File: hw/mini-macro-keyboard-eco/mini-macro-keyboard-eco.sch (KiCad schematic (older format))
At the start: 39 parts, among them J0 USB, J1 DEBUG_SWD, SW0 BOOT, SW1 SW_Cherry_MX_1.00u_PCB, SW2 SW_Cherry_MX_1.00u_PCB, SW3 SW_Cherry_MX_1.00u_PCB, SW4 RESET, SW5 LAYOUT, SW6 BACKLIGHT, U1 USBLC6-2SC6, U2 XC6206P322MR, U3 STM32F070F6P6, Y1 16 MHz

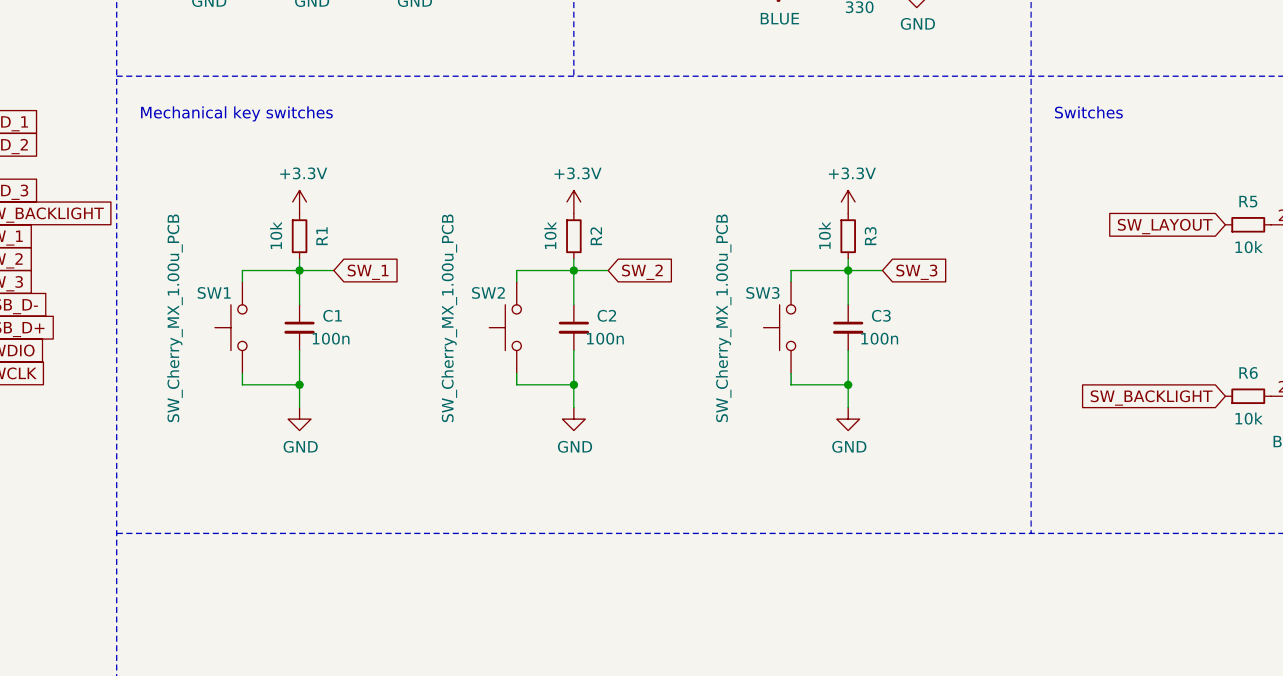
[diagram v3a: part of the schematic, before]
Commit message: fix(hw): remove debounce circuit from the mechanical switches
Signed-off-by: Ivan Kovalenko <s1ckretbox@gmail.com>
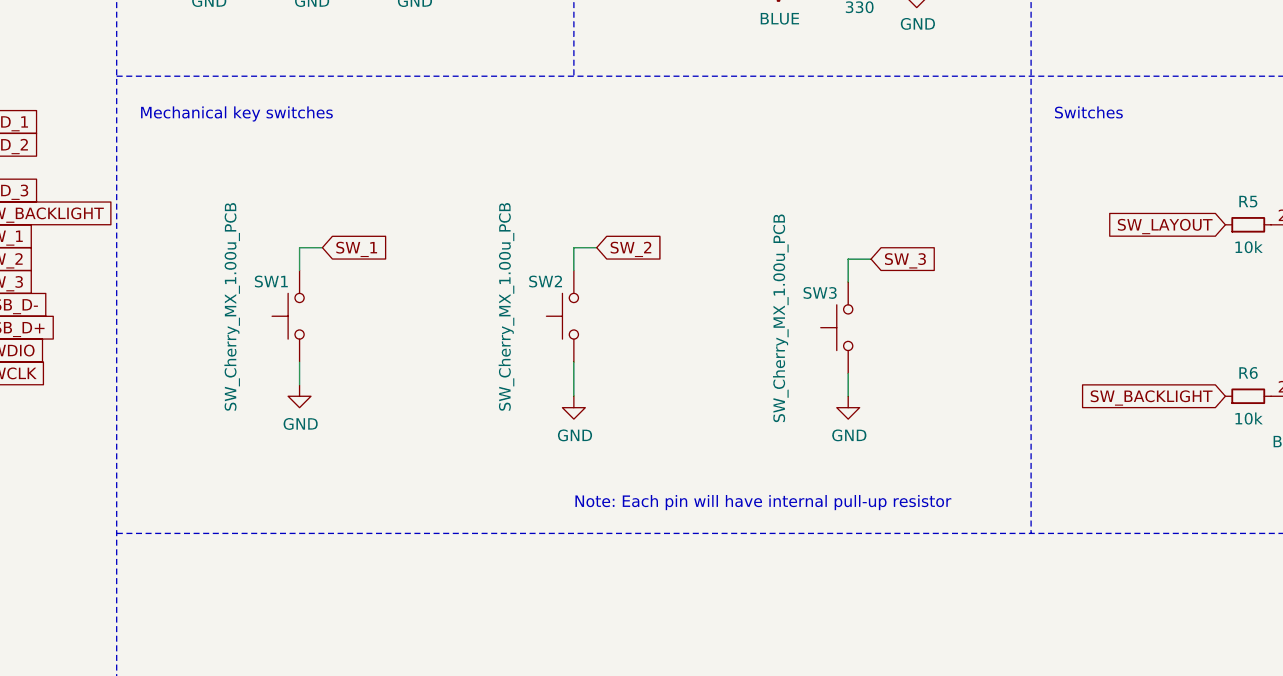
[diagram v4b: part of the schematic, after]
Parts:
- removed C1, C2, C3: 100n, Capacitor_SMD:C_0402_1005Metric, symbol mini-macro-keyboard-eco-rescue:C_Small-Device
- removed R1, R2, R3: 10k, Resistor_SMD:R_0402_1005Metric, symbol mini-macro-keyboard-eco-rescue:R_Small-Device
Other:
- note added: "Note: Each pin will have internal pull-up resistor"
- moved on the sheet: SW1, SW2, SW3
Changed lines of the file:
@@
 Wire Notes Line
 	5000 500  5000 7800
-Text GLabel 5950 2850 2    50   Input ~ 0
+Text GLabel 5900 2750 2    50   Input ~ 0
 SW_1
-$Comp
-L mini-macro-keyboard-eco-rescue:+3.3V-power #PWR0125
-U 1 1 5FFBA660
-P 5800 2600
-F 0 "#PWR0125" H 5800 2450 50  0001 C CNN
-F 1 "+3.3V" H 5815 2773 50  0000 C CNN
-F 2 "" H 5800 2600 50  0001 C CNN
-F 3 "" H 5800 2600 50  0001 C CNN
-	1    5800 2600
-	1    0    0    -1
-$EndComp
-Wire Wire Line
-	5800 3350 5800 3450
-Connection ~ 5800 3350
-Wire Wire Line
-	5550 3350 5800 3350
-Wire Wire Line
-	5550 3300 5550 3350
-Wire Wire Line
-	5550 2850 5550 2900
-Wire Wire Line
-	5800 2850 5550 2850
-Wire Wire Line
-	5800 3200 5800 3350
-$Comp
-L mini-macro-keyboard-eco-rescue:R_Small-Device R1
-U 1 1 5FFBA64D
-P 5800 2700
-F 0 "R1" V 5900 2700 50  0000 C CNN
-F 1 "10k" V 5700 2700 50  0000 C CNN
-F 2 "Resistor_SMD:R_0402_1005Metric" H 5800 2700 50  0001 C CNN
-F 3 "~" H 5800 2700 50  0001 C CNN
-	1    5800 2700
-	1    0    0    -1
-$EndComp
-Wire Wire Line
-	5800 2850 5950 2850
-Connection ~ 5800 2850
-Wire Wire Line
-	5800 3000 5800 2850
 $Comp
 L mini-macro-keyboard-eco-rescue:GND-power #PWR0126
 U 1 1 5FFBA643
-P 5800 3450
-F 0 "#PWR0126" H 5800 3200 50  0001 C CNN
-F 1 "GND" H 5805 3277 50  0000 C CNN
-F 2 "" H 5800 3450 50  0001 C CNN
-F 3 "" H 5800 3450 50  0001 C CNN
-	1    5800 3450
-	1    0    0    -1
-$EndComp
-Wire Wire Line
-	5800 2800 5800 2850
-$Comp
-L mini-macro-keyboard-eco-rescue:C_Small-Device C1
-U 1 1 5FFBA63C
-P 5800 3100
-F 0 "C1" H 5900 3150 50  0000 L CNN
-F 1 "100n" H 5850 3050 50  0000 L CNN
-F 2 "Capacitor_SMD:C_0402_1005Metric" H 5800 3100 50  0001 C CNN
-F 3 "~" H 5800 3100 50  0001 C CNN
-	1    5800 3100
-	1    0    0    -1
-$EndComp
-Text GLabel 8350 2850 2    50   Input ~ 0
+P 5800 3350
+F 0 "#PWR0126" H 5800 3100 50  0001 C CNN
+F 1 "GND" H 5805 3177 50  0000 C CNN
+F 2 "" H 5800 3350 50  0001 C CNN
+F 3 "" H 5800 3350 50  0001 C CNN
+	1    5800 3350
+	1    0    0    -1
+$EndComp
+Text GLabel 8300 2800 2    50   Input ~ 0
 SW_3
-$Comp
-L mini-macro-keyboard-eco-rescue:+3.3V-power #PWR0127
-U 1 1 5FFC23F4
-P 8200 2600
-F 0 "#PWR0127" H 8200 2450 50  0001 C CNN
-F 1 "+3.3V" H 8215 2773 50  0000 C CNN
-F 2 "" H 8200 2600 50  0001 C CNN
-F 3 "" H 8200 2600 50  0001 C CNN
-	1    8200 2600
-	1    0    0    -1
-$EndComp
-Wire Wire Line
-	8200 3350 8200 3450
-Connection ~ 8200 3350
-Wire Wire Line
-	7950 3350 8200 3350
-Wire Wire Line
-	7950 3300 7950 3350
-Wire Wire Line
-	7950 2850 7950 2900
-Wire Wire Line
-	8200 2850 7950 2850
-Wire Wire Line
-	8200 3200 8200 3350
-$Comp
-L mini-macro-keyboard-eco-rescue:R_Small-Device R3
-U 1 1 5FFC23E1
-P 8200 2700
-F 0 "R3" V 8300 2700 50  0000 C CNN
-F 1 "10k" V 8100 2700 50  0000 C CNN
-F 2 "Resistor_SMD:R_0402_1005Metric" H 8200 2700 50  0001 C CNN
-F 3 "~" H 8200 2700 50  0001 C CNN
-	1    8200 2700
-	1    0    0    -1
-$EndComp
-Wire Wire Line
-	8200 2850 8350 2850
-Connection ~ 8200 2850
-Wire Wire Line
-	8200 3000 8200 2850
 $Comp
 L mini-macro-keyboard-eco-rescue:GND-power #PWR0128
 U 1 1 5FFC23D8
-P 8200 3450
-F 0 "#PWR0128" H 8200 3200 50  0001 C CNN
-F 1 "GND" H 8205 3277 50  0000 C CNN
-F 2 "" H 8200 3450 50  0001 C CNN
-F 3 "" H 8200 3450 50  0001 C CNN
-	1    8200 3450
-	1    0    0    -1
-$EndComp
-Wire Wire Line
-	8200 2800 8200 2850
-$Comp
-L mini-macro-keyboard-eco-rescue:C_Small-Device C3
-U 1 1 5FFC23D1
-P 8200 3100
-F 0 "C3" H 8300 3150 50  0000 L CNN
-F 1 "100n" H 8250 3050 50  0000 L CNN
-F 2 "Capacitor_SMD:C_0402_1005Metric" H 8200 3100 50  0001 C CNN
-F 3 "~" H 8200 3100 50  0001 C CNN
-	1    8200 3100
-	1    0    0    -1
-$EndComp
-Text GLabel 7150 2850 2    50   Input ~ 0
+P 8200 3400
+F 0 "#PWR0128" H 8200 3150 50  0001 C CNN
+F 1 "GND" H 8205 3227 50  0000 C CNN
+F 2 "" H 8200 3400 50  0001 C CNN
+F 3 "" H 8200 3400 50  0001 C CNN
+	1    8200 3400
+	1    0    0    -1
+$EndComp
+Text GLabel 7100 2750 2    50   Input ~ 0
 SW_2
-$Comp
-L mini-macro-keyboard-eco-rescue:+3.3V-power #PWR0129
-U 1 1 5FFBFB0E
-P 7000 2600
-F 0 "#PWR0129" H 7000 2450 50  0001 C CNN
-F 1 "+3.3V" H 7015 2773 50  0000 C CNN
-F 2 "" H 7000 2600 50  0001 C CNN
-F 3 "" H 7000 2600 50  0001 C CNN
-	1    7000 2600
-	1    0    0    -1
-$EndComp
-Wire Wire Line
-	7000 3350 7000 3450
-Connection ~ 7000 3350
-Wire Wire Line
-	6750 3350 7000 3350
-Wire Wire Line
-	6750 3300 6750 3350
-Wire Wire Line
-	6750 2850 6750 2900
-Wire Wire Line
-	7000 2850 6750 2850
-Wire Wire Line
-	7000 3200 7000 3350
-$Comp
-L mini-macro-keyboard-eco-rescue:R_Small-Device R2
-U 1 1 5FFBFAFB
-P 7000 2700
-F 0 "R2" V 7100 2700 50  0000 C CNN
-F 1 "10k" V 6900 2700 50  0000 C CNN
-F 2 "Resistor_SMD:R_0402_1005Metric" H 7000 2700 50  0001 C CNN
-F 3 "~" H 7000 2700 50  0001 C CNN
-	1    7000 2700
-	1    0    0    -1
-$EndComp
-Wire Wire Line
-	7000 2850 7150 2850
-Connection ~ 7000 2850
-Wire Wire Line
-	7000 3000 7000 2850
 $Comp
 L mini-macro-keyboard-eco-rescue:GND-power #PWR0130
 U 1 1 5FFBFAF2
-P 7000 3450
-F 0 "#PWR0130" H 7000 3200 50  0001 C CNN
-F 1 "GND" H 7005 3277 50  0000 C CNN
-F 2 "" H 7000 3450 50  0001 C CNN
-F 3 "" H 7000 3450 50  0001 C CNN
-	1    7000 3450
-	1    0    0    -1
-$EndComp
-Wire Wire Line
-	7000 2800 7000 2850
-$Comp
-L mini-macro-keyboard-eco-rescue:C_Small-Device C2
-U 1 1 5FFBFAEB
-P 7000 3100
-F 0 "C2" H 7100 3150 50  0000 L CNN
-F 1 "100n" H 7050 3050 50  0000 L CNN
-F 2 "Capacitor_SMD:C_0402_1005Metric" H 7000 3100 50  0001 C CNN
-F 3 "~" H 7000 3100 50  0001 C CNN
-	1    7000 3100
+P 7000 3400
+F 0 "#PWR0130" H 7000 3150 50  0001 C CNN
+F 1 "GND" H 7005 3227 50  0000 C CNN
+F 2 "" H 7000 3400 50  0001 C CNN
+F 3 "" H 7000 3400 50  0001 C CNN
+	1    7000 3400
 	1    0    0    -1
 $EndComp
@@
 L mini-macro-keyboard-eco-rescue:SW_Push-Switch SW3
 U 1 1 5FFC23E7
-P 7950 3100
-F 0 "SW3" V 8100 3300 50  0000 R CNN
-F 1 "SW_Cherry_MX_1.00u_PCB" H 8450 3400 50  0000 R CNN
-F 2 "Button_Switch_Keyboard:SW_Cherry_MX_1.00u_PCB" H 7950 3300 50  0001 C CNN
-F 3 "~" H 7950 3300 50  0001 C CNN
-	1    7950 3100
+P 8200 3100
+F 0 "SW3" V 8350 3300 50  0000 R CNN
+F 1 "SW_Cherry_MX_1.00u_PCB" H 8700 3400 50  0000 R CNN
+F 2 "Button_Switch_Keyboard:SW_Cherry_MX_1.00u_PCB" H 8200 3300 50  0001 C CNN
+F 3 "~" H 8200 3300 50  0001 C CNN
+	1    8200 3100
 	0    -1   -1   0
 $EndComp
@@
 L mini-macro-keyboard-eco-rescue:SW_Push-Switch SW2
 U 1 1 5FFBFB01
-P 6750 3100
-F 0 "SW2" V 6900 3300 50  0000 R CNN
-F 1 "SW_Cherry_MX_1.00u_PCB" H 7250 3400 50  0000 R CNN
-F 2 "Button_Switch_Keyboard:SW_Cherry_MX_1.00u_PCB" H 6750 3300 50  0001 C CNN
-F 3 "~" H 6750 3300 50  0001 C CNN
-	1    6750 3100
+P 7000 3050
+F 0 "SW2" V 7150 3250 50  0000 R CNN
+F 1 "SW_Cherry_MX_1.00u_PCB" H 7500 3350 50  0000 R CNN
+F 2 "Button_Switch_Keyboard:SW_Cherry_MX_1.00u_PCB" H 7000 3250 50  0001 C CNN
+F 3 "~" H 7000 3250 50  0001 C CNN
+	1    7000 3050
 	0    -1   -1   0
 $EndComp
@@
 L mini-macro-keyboard-eco-rescue:SW_Push-Switch SW1
 U 1 1 5FFBA653
-P 5550 3100
-F 0 "SW1" V 5700 3300 50  0000 R CNN
-F 1 "SW_Cherry_MX_1.00u_PCB" H 6050 3400 50  0000 R CNN
-F 2 "Button_Switch_Keyboard:SW_Cherry_MX_1.00u_PCB" H 5550 3300 50  0001 C CNN
-F 3 "~" H 5550 3300 50  0001 C CNN
-	1    5550 3100
+P 5800 3050
+F 0 "SW1" V 5950 3250 50  0000 R CNN
+F 1 "SW_Cherry_MX_1.00u_PCB" H 6300 3350 50  0000 R CNN
+F 2 "Button_Switch_Keyboard:SW_Cherry_MX_1.00u_PCB" H 5800 3250 50  0001 C CNN
+F 3 "~" H 5800 3250 50  0001 C CNN
+	1    5800 3050
 	0    -1   -1   0
 $EndComp
+Wire Wire Line
+	5800 3350 5800 3250
+Wire Wire Line
+	5900 2750 5800 2750
+Wire Wire Line
+	5800 2750 5800 2850
+Wire Wire Line
+	7100 2750 7000 2750
+Wire Wire Line
+	7000 2750 7000 2850
+Wire Wire Line
+	7000 3400 7000 3250
+Wire Wire Line
+	8300 2800 8200 2800
+Wire Wire Line
+	8200 2800 8200 2900
+Wire Wire Line
+	8200 3300 8200 3400
+Text Notes 7000 3900 0    50   ~ 0
+Note: Each pin will have internal pull-up resistor
 $EndSCHEMATC

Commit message: feat(hw)!: remove reset push button
BREAKING CHANGE:
I remove the reset schematic becauce it uses a lot of space and
I won't mess with usb bootloaders in the future. Also I don't know
how to update software on the MCU in the user-friendly manner.

Signed-off-by: Ivan Kovalenko <s1ckretbox@gmail.com>
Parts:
- removed C4: 100n, Capacitor_SMD:C_0402_1005Metric, symbol mini-macro-keyboard-eco-rescue:C_Small-Device
- removed R4: 10k, Resistor_SMD:R_0402_1005Metric, symbol mini-macro-keyboard-eco-rescue:R_Small-Device
- removed SW4: RESET, Button_Switch_THT:SW_PUSH_6mm, symbol mini-macro-keyboard-eco-rescue:SW_Push-Switch
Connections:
- net NRST: no longer names the net of U3.4 (NRST)
- no-connect marks 2 -> 3
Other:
- note removed: "Reset push button"
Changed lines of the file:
@@
-$EndComp
-$Comp
-L mini-macro-keyboard-eco-rescue:C_Small-Device C4
-U 1 1 5FF9DDD1
-P 1500 1500
-F 0 "C4" H 1600 1550 50  0000 L CNN
-F 1 "100n" H 1550 1450 50  0000 L CNN
-F 2 "Capacitor_SMD:C_0402_1005Metric" H 1500 1500 50  0001 C CNN
-F 3 "~" H 1500 1500 50  0001 C CNN
-	1    1500 1500
-	1    0    0    -1
 $EndComp
 $Comp
@@
 Text GLabel 3050 2400 0    50   Input ~ 0
 BOOT0
-Text GLabel 3050 2200 0    50   Input ~ 0
-NRST
-Wire Wire Line
-	1500 1200 1500 1250
-$Comp
-L mini-macro-keyboard-eco-rescue:GND-power #PWR0106
-U 1 1 5FFEBFB1
-P 1500 1850
-F 0 "#PWR0106" H 1500 1600 50  0001 C CNN
-F 1 "GND" H 1505 1677 50  0000 C CNN
-F 2 "" H 1500 1850 50  0001 C CNN
-F 3 "" H 1500 1850 50  0001 C CNN
-	1    1500 1850
-	1    0    0    -1
-$EndComp
-Wire Wire Line
-	1500 1400 1500 1250
-Connection ~ 1500 1250
-Text GLabel 1650 1250 2    50   Input ~ 0
-NRST
-Wire Wire Line
-	1500 1250 1650 1250
 Text GLabel 3050 3000 0    50   Input ~ 0
 OSC_IN
@@
 $EndComp
 $Comp
-L mini-macro-keyboard-eco-rescue:R_Small-Device R4
-U 1 1 5FFE7355
-P 1500 1100
-F 0 "R4" V 1600 1100 50  0000 C CNN
-F 1 "10k" V 1400 1100 50  0000 C CNN
-F 2 "Resistor_SMD:R_0402_1005Metric" H 1500 1100 50  0001 C CNN
-F 3 "~" H 1500 1100 50  0001 C CNN
-	1    1500 1100
-	1    0    0    -1
-$EndComp
-$Comp
 L mini-macro-keyboard-eco-rescue:R_Small-Device R7
 U 1 1 60011E97
@@
 F 3 "" H 9700 1450 50  0001 C CNN
 	1    9700 1450
-	1    0    0    -1
-$EndComp
-$Comp
-L mini-macro-keyboard-eco-rescue:SW_Push-Switch SW4
-U 1 1 5FFA57A7
-P 1250 1500
-F 0 "SW4" V 1400 1700 50  0000 R CNN
-F 1 "RESET" V 1100 1850 50  0000 R CNN
-F 2 "Button_Switch_THT:SW_PUSH_6mm" H 1250 1700 50  0001 C CNN
-F 3 "~" H 1250 1700 50  0001 C CNN
-	1    1250 1500
-	0    -1   -1   0
-$EndComp
-Wire Wire Line
-	1500 1600 1500 1750
-Wire Wire Line
-	1500 1250 1250 1250
-Wire Wire Line
-	1250 1250 1250 1300
-Wire Wire Line
-	1250 1700 1250 1750
-Wire Wire Line
-	1250 1750 1500 1750
-Connection ~ 1500 1750
-Wire Wire Line
-	1500 1750 1500 1850
-$Comp
-L mini-macro-keyboard-eco-rescue:+3.3V-power #PWR0123
-U 1 1 5FFB05C0
-P 1500 1000
-F 0 "#PWR0123" H 1500 850 50  0001 C CNN
-F 1 "+3.3V" H 1515 1173 50  0000 C CNN
-F 2 "" H 1500 1000 50  0001 C CNN
-F 3 "" H 1500 1000 50  0001 C CNN
-	1    1500 1000
 	1    0    0    -1
 $EndComp
@@
 Text Notes 2600 650  0    50   ~ 0
 STM32 Microcontroller\n
-Text Notes 550  650  0    50   ~ 0
-Reset push button
 Text Notes 7100 650  0    50   ~ 0
 LEDs\n
@@
 Text Notes 7000 3900 0    50   ~ 0
 Note: Each pin will have internal pull-up resistor
+NoConn ~ 3050 2200
 $EndSCHEMATC

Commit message: feat(hw)!: remove boot switch
I have removed boot switch because I don't expect to use another
bootloaders

Signed-off-by: Ivan Kovalenko <s1ckretbox@gmail.com>
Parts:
- removed R0: 10k, Resistor_SMD:R_0402_1005Metric, symbol mini-macro-keyboard-eco-rescue:R_Small-Device
- removed SW0: BOOT, Button_Switch_SMD:SW_SPDT_PCM12, symbol mini-macro-keyboard-eco-rescue:SW_SPDT-Switch
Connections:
- net BOOT0 is gone; now on net GND: U3.1 (BOOT0)
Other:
- note removed: "Boot switch"
- moved on the sheet: C8, C9, J0, R7, U1, Y1

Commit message: feat(hw): reanotate schematic
Signed-off-by: Ivan Kovalenko <s1ckretbox@gmail.com>
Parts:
- renumbered C9 to C0, C8 to C1, C5 to C2, C6 to C3, C7 to C4, C10 to C5, C11 to C6, C0 to C7, R7 to R0, R11 to R1, R12 to R2, R13 to R3
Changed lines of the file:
@@
 $EndComp
 $Comp
-L mini-macro-keyboard-eco-rescue:C_Small-Device C5
+L mini-macro-keyboard-eco-rescue:C_Small-Device C2
 U 1 1 5FF9BD70
 P 3300 1200
-F 0 "C5" H 3400 1250 50  0000 L CNN
+F 0 "C2" H 3400 1250 50  0000 L CNN
 F 1 "100n" H 3350 1150 50  0000 L CNN
 F 2 "Capacitor_SMD:C_0402_1005Metric" H 3300 1200 50  0001 C CNN
@@
 $EndComp
 $Comp
-L mini-macro-keyboard-eco-rescue:C_Small-Device C6
+L mini-macro-keyboard-eco-rescue:C_Small-Device C3
 U 1 1 5FF9D075
 P 3600 1200
-F 0 "C6" H 3700 1250 50  0000 L CNN
+F 0 "C3" H 3700 1250 50  0000 L CNN
 F 1 "100n" H 3650 1150 50  0000 L CNN
 F 2 "Capacitor_SMD:C_0402_1005Metric" H 3600 1200 50  0001 C CNN
@@
 $EndComp
 $Comp
-L mini-macro-keyboard-eco-rescue:C_Small-Device C7
+L mini-macro-keyboard-eco-rescue:C_Small-Device C4
 U 1 1 5FF9E127
 P 3950 1200
-F 0 "C7" H 4050 1250 50  0000 L CNN
+F 0 "C4" H 4050 1250 50  0000 L CNN
 F 1 "4.7u" H 4000 1150 50  0000 L CNN
 F 2 "Capacitor_SMD:C_0402_1005Metric" H 3950 1200 50  0001 C CNN
@@
 OSC_OUT
 $Comp
-L mini-macro-keyboard-eco-rescue:C_Small-Device C9
+L mini-macro-keyboard-eco-rescue:C_Small-Device C0
 U 1 1 6000E4D6
 P 1100 3300
-F 0 "C9" H 850 3250 50  0000 L CNN
+F 0 "C0" H 850 3250 50  0000 L CNN
 F 1 "12p" H 850 3350 50  0000 L CNN
 F 2 "Capacitor_SMD:C_0402_1005Metric" H 1100 3300 50  0001 C CNN
@@
 $EndComp
 $Comp
-L mini-macro-keyboard-eco-rescue:R_Small-Device R7
+L mini-macro-keyboard-eco-rescue:R_Small-Device R0
 U 1 1 60011E97
 P 1650 2700
-F 0 "R7" H 1800 2750 50  0000 C CNN
+F 0 "R0" H 1800 2750 50  0000 C CNN
 F 1 "47" H 1800 2650 50  0000 C CNN
 F 2 "Resistor_SMD:R_0402_1005Metric" H 1650 2700 50  0001 C CNN
@@
 $EndComp
 $Comp
-L mini-macro-keyboard-eco-rescue:R_Small-Device R11
+L mini-macro-keyboard-eco-rescue:R_Small-Device R1
 U 1 1 6009B719
 P 8250 900
-F 0 "R11" V 8350 900 50  0000 C CNN
+F 0 "R1" V 8350 900 50  0000 C CNN
 F 1 "330" V 8150 900 50  0000 C CNN
 F 2 "Resistor_SMD:R_0603_1608Metric" H 8250 900 50  0001 C CNN
@@
 $EndComp
 $Comp
-L mini-macro-keyboard-eco-rescue:R_Small-Device R12
+L mini-macro-keyboard-eco-rescue:R_Small-Device R2
 U 1 1 600AA3E1
 P 8250 1250
-F 0 "R12" V 8350 1250 50  0000 C CNN
+F 0 "R2" V 8350 1250 50  0000 C CNN
 F 1 "330" V 8150 1250 50  0000 C CNN
 F 2 "Resistor_SMD:R_0603_1608Metric" H 8250 1250 50  0001 C CNN
@@
 $EndComp
 $Comp
-L mini-macro-keyboard-eco-rescue:R_Small-Device R13
+L mini-macro-keyboard-eco-rescue:R_Small-Device R3
 U 1 1 600AC5B9
 P 8250 1600
-F 0 "R13" V 8350 1600 50  0000 C CNN
+F 0 "R3" V 8350 1600 50  0000 C CNN
 F 1 "330" V 8150 1600 50  0000 C CNN
 F 2 "Resistor_SMD:R_0603_1608Metric" H 8250 1600 50  0001 C CNN
@@
 SWCLK
 $Comp
-L mini-macro-keyboard-eco-rescue:C_Small-Device C0
+L mini-macro-keyboard-eco-rescue:C_Small-Device C7
 U 1 1 600C2115
 P 9700 1200
-F 0 "C0" H 9800 1250 50  0000 L CNN
+F 0 "C7" H 9800 1250 50  0000 L CNN
 F 1 "100n" H 9750 1150 50  0000 L CNN
 F 2 "Capacitor_SMD:C_0402_1005Metric" H 9700 1200 50  0001 C CNN
@@
 $EndComp
 $Comp
-L mini-macro-keyboard-eco-rescue:C_Small-Device C10
+L mini-macro-keyboard-eco-rescue:C_Small-Device C5
 U 1 1 60114EAE
 P 5400 1400
-F 0 "C10" H 5450 1500 50  0000 L CNN
+F 0 "C5" H 5450 1500 50  0000 L CNN
 F 1 "1u" H 5500 1300 50  0000 L CNN
 F 2 "Capacitor_SMD:C_0402_1005Metric" H 5400 1400 50  0001 C CNN
@@
 $EndComp
 $Comp
-L mini-macro-keyboard-eco-rescue:C_Small-Device C11
+L mini-macro-keyboard-eco-rescue:C_Small-Device C6
 U 1 1 6011562F
 P 6300 1400
-F 0 "C11" H 6350 1500 50  0000 L CNN
+F 0 "C6" H 6350 1500 50  0000 L CNN
 F 1 "1u" H 6400 1300 50  0000 L CNN
 F 2 "Capacitor_SMD:C_0402_1005Metric" H 6300 1400 50  0001 C CNN
@@
 $EndComp
 $Comp
-L mini-macro-keyboard-eco-rescue:C_Small-Device C8
+L mini-macro-keyboard-eco-rescue:C_Small-Device C1
 U 1 1 5FFE79A1
 P 1650 3300
-F 0 "C8" H 1450 3250 50  0000 L CNN
+F 0 "C1" H 1450 3250 50  0000 L CNN
 F 1 "12p" H 1400 3350 50  0000 L CNN
 F 2 "Capacitor_SMD:C_0402_1005Metric" H 1650 3300 50  0001 C CNN
@@
 NoConn ~ 3050 2200
 $Comp
-L mini-macro-keyboard-eco-rescue:GND-power #PWR?
+L mini-macro-keyboard-eco-rescue:GND-power #PWR0104
 U 1 1 600CAED8
 P 2950 2500
-F 0 "#PWR?" H 2950 2250 50  0001 C CNN
+F 0 "#PWR0104" H 2950 2250 50  0001 C CNN
 F 1 "GND" H 2955 2327 50  0000 C CNN
 F 2 "" H 2950 2500 50  0001 C CNN
